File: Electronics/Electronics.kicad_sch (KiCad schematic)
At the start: 10 parts, among them M1 Motor_Servo, SW1 SW_SPDT

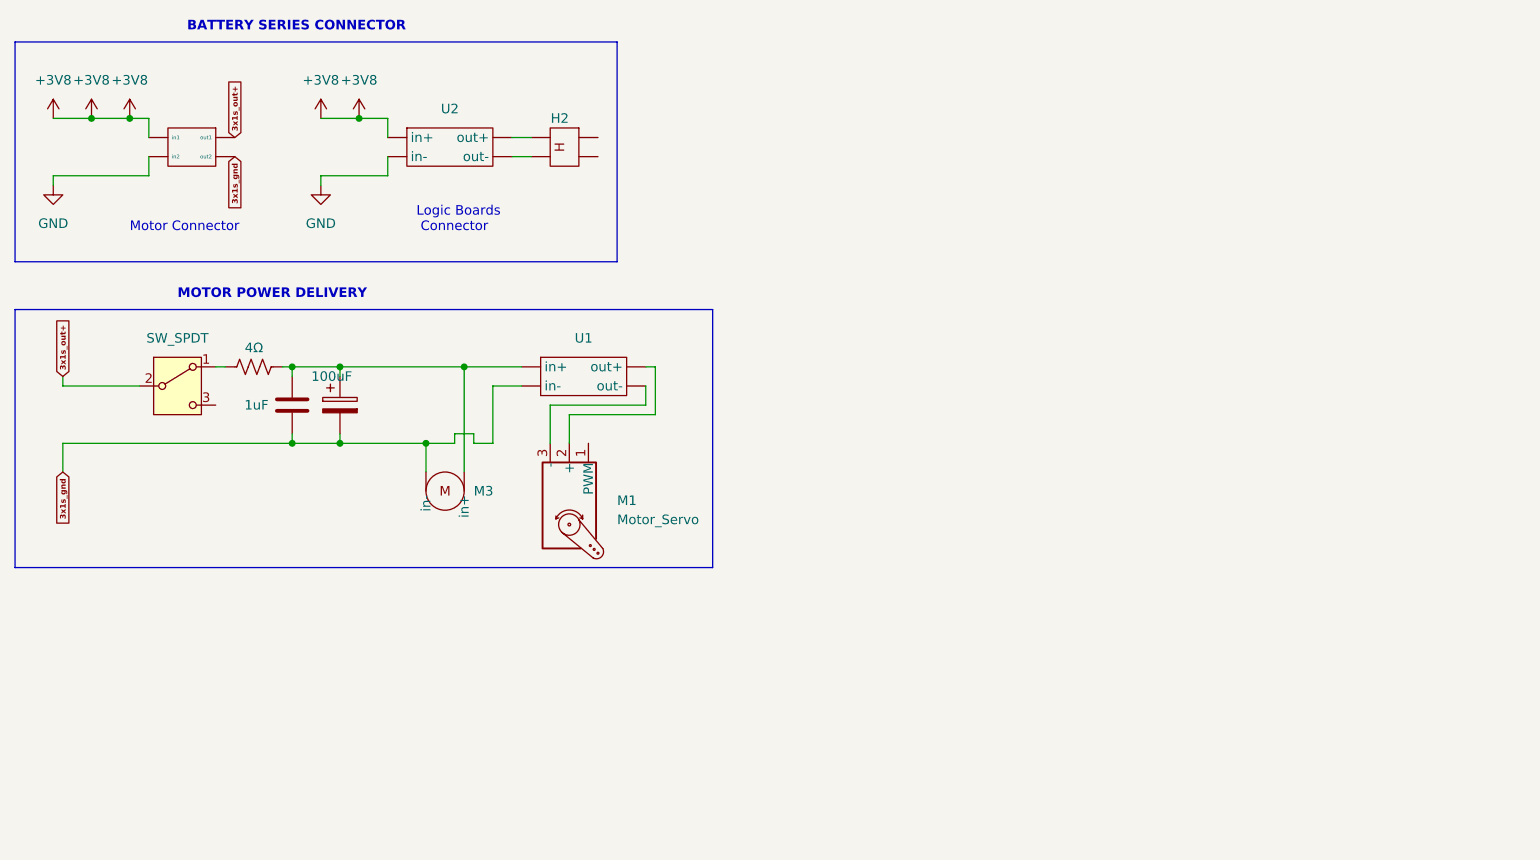
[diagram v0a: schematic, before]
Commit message: changes to schematics and code
Finalized schematics. Started implementation of server code.
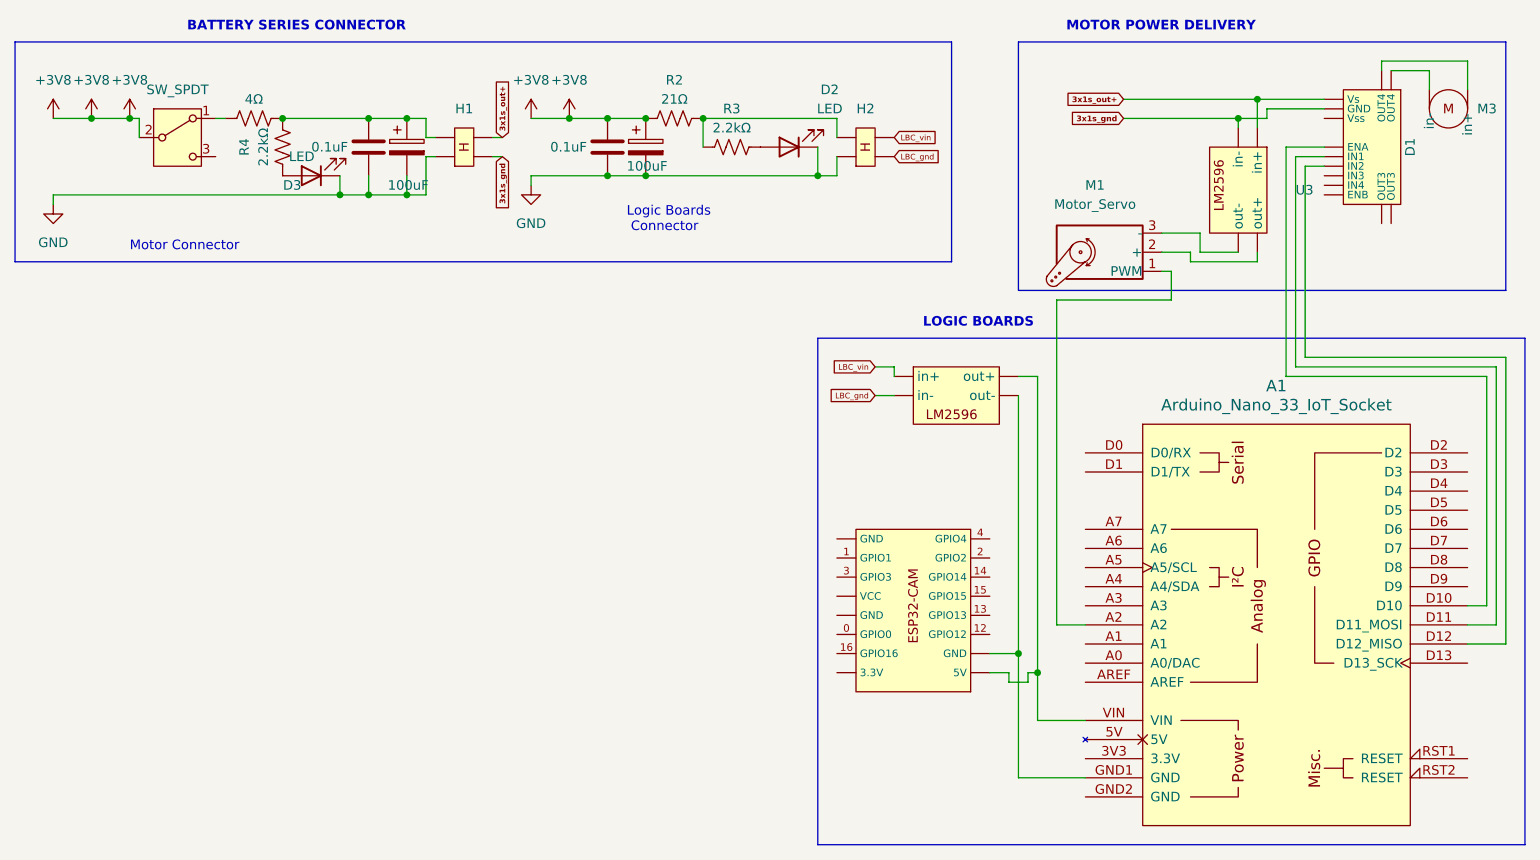
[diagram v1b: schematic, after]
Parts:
- removed C2: 100uF, symbol Device:C_Polarized
- removed C3: 1uF, symbol Device:C
- removed U2: ~, symbol additional_symbols:LM2596
- added A1: Arduino_Nano_33_IoT_Socket, PCM_arduino-library:Arduino_Nano_33_IoT_Socket, symbol PCM_arduino-library:Arduino_Nano_33_IoT_Socket
- added C1, C5: 0.1uF, symbol Device:C
- added C4, C6: 100uF, symbol Device:C_Polarized
- added D1: ~, symbol additional_symbols:L298N_Module
- added D2, D3: LED, symbol Device:LED
- added M2: ~, symbol additional_symbols:ESP32-CAM
- added R2: 21Ω, symbol Device:R_US
- added R3, R4: 2.2kΩ, symbol Device:R_US
- added U3: ~, symbol additional_symbols:LM2596
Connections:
- net +3V8: now also SW1.2 (B), C1.1, C4.1, R2.1; no longer H1. (out2)
- net 3x1s_gnd: now also D1. (Vss), U3. (out-); no longer M3. (in-), U1. (out-)
- net 3x1s_out+: now also D1. (Vss), U3. (out-); no longer SW1.2 (B)
- net GND: now also H2., C1.2, C4.2, C5.2, C6.2, D2.1 (K), D3.1 (K)
- net LBC_vin: now reaches H2.
- net LBC_vin: now also U1. (out-)
- net at M1.2 (+): now also U3. (out-); no longer U1. (out-)
- net at M1.3 (-): now also U3. (out-); no longer U1. (out-)
- net at M1.1 (PWM): now also A1.A2
- new net: H2., R2.2, R3.1
- new net: D3.2 (A), R4.1
- new net: C5.1, C6.1, H1., R1.2, R4.2
- new net: D1. (Vss), M3. (in-) (x2)
- new net: D2.2 (A), R3.2
- new net: A1.D10, D1. (Vss)
- new net: A1.D11 (D11_MOSI), D1. (Vss)
- new net: A1.D12 (D12_MISO), D1. (Vss)
- new net: A1.GND1 (GND), M2. (VCC), U1. (out-)
- new net: A1.VIN, M2. (VCC), U1. (out-)
- new net LBC_gnd: H2., U1. (out-)
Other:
- note added: "LOGIC BOARDS"
- moved on the sheet: M1, M3
